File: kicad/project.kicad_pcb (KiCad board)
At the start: 2 copper layers, 58 x 58 mm, 40 parts, among them J1 Conn_01x05, J2 Conn_01x01, Q1 SI2323CDS, SW1 SW_SPDT, SW2 SW_SPDT, SW3 SW_Push, U1 STM32L031F4Px

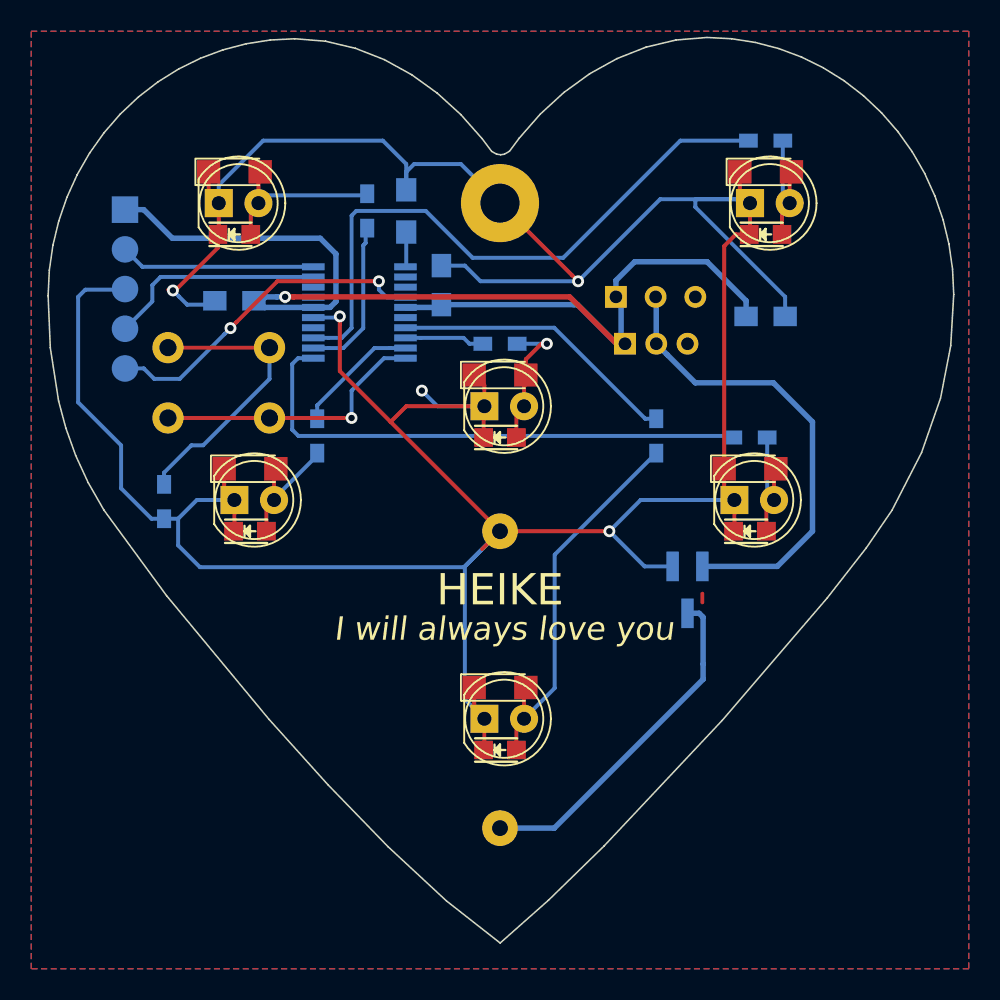
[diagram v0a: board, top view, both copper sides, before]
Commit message: Also fit the premade mould from China
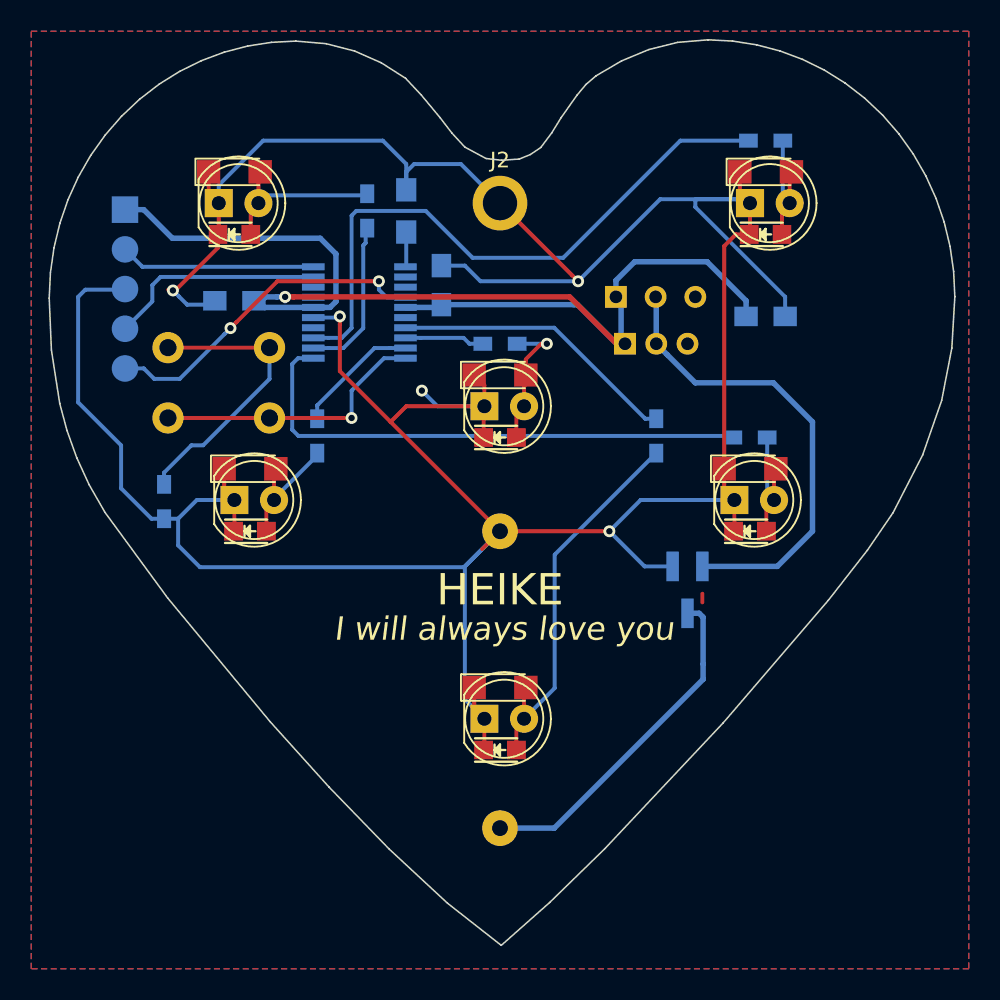
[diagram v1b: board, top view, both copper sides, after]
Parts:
- J1: footprint SWD_Header -> theapi:SWD_Header
- J2: footprint Mounting_Holes:MountingHole_2.5mm_Pad -> Mounting_Holes:MountingHole_2.2mm_M2_ISO7380_Pad
- moved REF** 15.9 mm to (140.5, 88.2)
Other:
- outline, holes or cut-outs redrawn

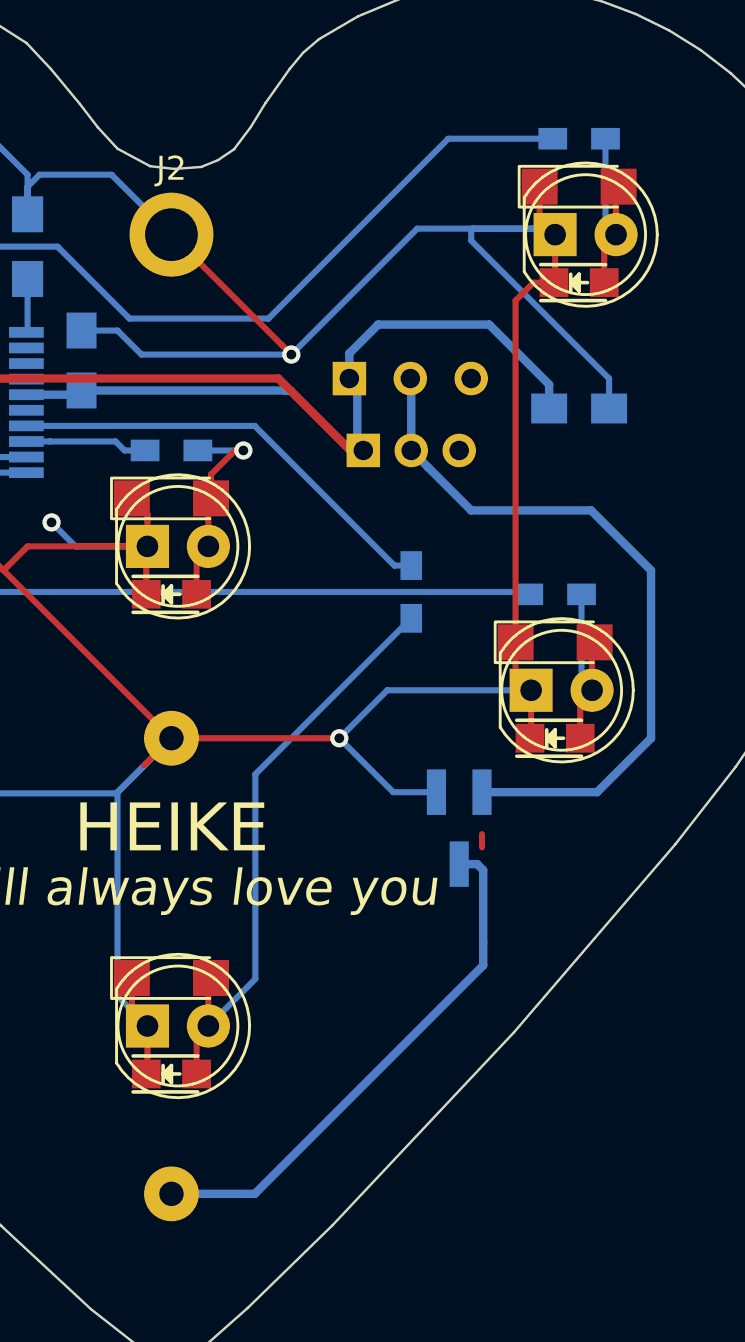
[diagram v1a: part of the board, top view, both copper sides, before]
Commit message: Moved the mosfet away from the battery
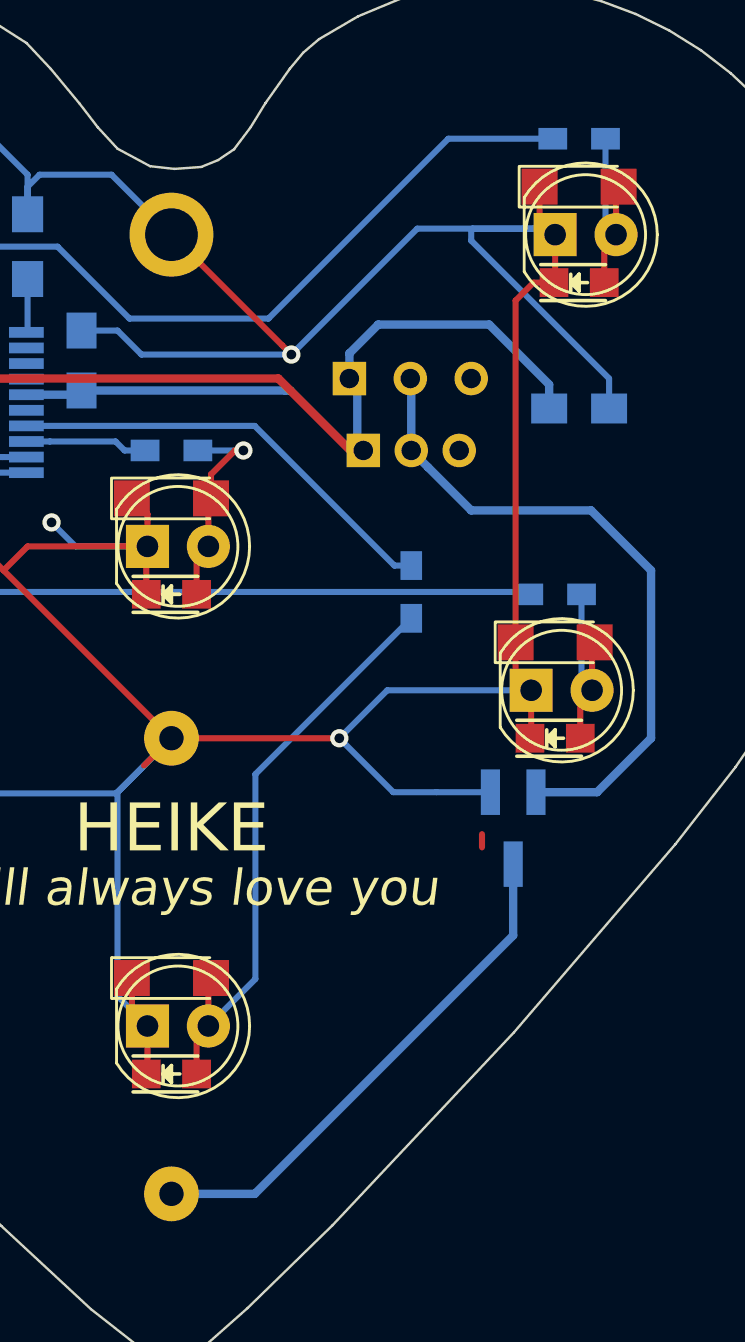
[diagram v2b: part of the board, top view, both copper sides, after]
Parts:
- moved Q1 2.25 mm to (144.2, 120.8)
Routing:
- net GND: track 233.2 -> 235.5 mm
- net /BATT_PROTECTED: track 30.1 -> 27.9 mm
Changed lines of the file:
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@@
     (links 69)
     (no_connects 0)
-    (area 101.09984 85.498481 159.15956 143.553153)
+    (area 97.899999 79.3 161.100001 148.700001)
     (thickness 1.6)
     (drawings 95)
-    (tracks 258)
+    (tracks 256)
     (zones 0)
     (modules 40)
@@
   )
   (module TO_SOT_Packages_SMD:SOT-23_Handsoldering (layer B.Cu)
-    (at 142 120.75 270)
+    (at 144.25 120.75 270)
     (descr "SOT-23, Handsoldering")
     (tags SOT-23)
@@
     (descr "Mounting Hole 2.2mm, M2, ISO7380")
     (tags "mounting hole 2.2mm m2 iso7380")
-    (fp_text reference J2 (at 0 -2.75) (layer F.SilkS)
+    (fp_text reference J2 (at 0 -2.75) (layer F.Fab)
       (effects (font (size 1 1) (thickness 0.15)))
     )
@@
   (gr_line (start 130 147) (end 130 82) (angle 90) (layer Cmts.User) (width 0.2))
   (segment (start 142.95 121) (end 142.95 121.55) (width 0.254) (layer F.Cu) (net 0))
+  (segment (start 141.05 119.25) (end 143.3 119.25) (width 0.254) (layer B.Cu) (net 1))
   (segment (start 145.096 95.75) (end 142.55 95.75) (width 0.254) (layer B.Cu) (net 1))
   (segment (start 142.55 95.75) (end 142.5 95.8) (width 0.254) (layer B.Cu) (net 1))
@@
   (segment (start 148.04902 98) (end 148.04902 96.49098) (width 0.254) (layer F.Cu) (net 22))
   (segment (start 148.04902 96.49098) (end 148.54 96) (width 0.254) (layer F.Cu) (net 22))
-  (segment (start 142.75 122.25) (end 142 122.25) (width 0.35) (layer B.Cu) (net 24))
   (segment (start 130 136) (end 133.475 136) (width 0.35) (layer B.Cu) (net 24))
-  (segment (start 133.475 136) (end 143 126.475) (width 0.35) (layer B.Cu) (net 24))
-  (segment (start 143 125.5) (end 143 122.5) (width 0.35) (layer B.Cu) (net 24))
-  (segment (start 143 122.5) (end 142.75 122.25) (width 0.35) (layer B.Cu) (net 24))
-  (segment (start 143 126.475) (end 143 125.5) (width 0.35) (layer B.Cu) (net 24))
+  (segment (start 133.475 136) (end 144.25 125.225) (width 0.35) (layer B.Cu) (net 24))
+  (segment (start 144.25 125.225) (end 144.25 122.25) (width 0.35) (layer B.Cu) (net 24))
   (segment (start 138 105) (end 137.75 104.75) (width 0.35) (layer B.Cu) (net 25))
   (segment (start 137.75 104.75) (end 137.75 102.33) (width 0.35) (layer B.Cu) (net 25))
@@
   (segment (start 120.5 109.75) (end 114.75 109.75) (width 0.254) (layer F.Cu) (net 28))
   (via (at 120.5 109.75) (size 0.762) (drill 0.4064) (layers F.Cu B.Cu) (net 28))
+  (segment (start 145.2 119.25) (end 147.75 119.25) (width 0.35) (layer B.Cu) (net 30))
   (segment (start 140 105) (end 140 102.04) (width 0.35) (layer B.Cu) (net 30))
   (segment (start 140 102.04) (end 139.96 102) (width 0.35) (layer B.Cu) (net 30))
-  (segment (start 142.95 119.25) (end 147.75 119.25) (width 0.35) (layer B.Cu) (net 30))
   (segment (start 150 110) (end 147.5 107.5) (width 0.35) (layer B.Cu) (net 30))
   (segment (start 147.75 119.25) (end 150 117) (width 0.35) (layer B.Cu) (net 30))

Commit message: Tidy up
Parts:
- R1: footprint Resistors_SMD:R_0805_HandSoldering -> Resistors_SMD:R_0603_HandSoldering
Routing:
- net (no net): track 0.55 -> 0.00 mm
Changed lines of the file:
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@@
     (thickness 1.6)
     (drawings 95)
-    (tracks 256)
+    (tracks 255)
     (zones 0)
     (modules 40)
@@
       (net 1 GND))
     (model LEDs.3dshapes/LED_0805.wrl
-      (at (xyz 0 0 0))
-      (scale (xyz 1 1 1))
-      (rotate (xyz 0 0 0))
-    )
-  )
-  (module Resistors_SMD:R_0805_HandSoldering (layer B.Cu)
-    (at 124 96.5 90)
-    (descr "Resistor SMD 0805, hand soldering")
-    (tags "resistor 0805")
-    (attr smd)
-    (fp_text reference R1 (at 0 2.1 90) (layer B.SilkS)
-      (effects (font (size 1 1) (thickness 0.15)) (justify mirror))
-    )
-    (fp_text value 10K (at 0 -2.1 90) (layer B.Fab)
-      (effects (font (size 1 1) (thickness 0.15)) (justify mirror))
-    )
-    (fp_line (start -1 -0.625) (end -1 0.625) (layer B.Fab) (width 0.1))
-    (fp_line (start 1 -0.625) (end -1 -0.625) (layer B.Fab) (width 0.1))
-    (fp_line (start 1 0.625) (end 1 -0.625) (layer B.Fab) (width 0.1))
-    (fp_line (start -1 0.625) (end 1 0.625) (layer B.Fab) (width 0.1))
-    (fp_line (start -2.4 1) (end 2.4 1) (layer B.CrtYd) (width 0.05))
-    (fp_line (start -2.4 -1) (end 2.4 -1) (layer B.CrtYd) (width 0.05))
-    (fp_line (start -2.4 1) (end -2.4 -1) (layer B.CrtYd) (width 0.05))
-    (fp_line (start 2.4 1) (end 2.4 -1) (layer B.CrtYd) (width 0.05))
-    (fp_line (start 0.6 -0.875) (end -0.6 -0.875) (layer B.SilkS) (width 0.15))
-    (fp_line (start -0.6 0.875) (end 0.6 0.875) (layer B.SilkS) (width 0.15))
-    (pad 1 smd rect (at -1.35 0 90) (size 1.5 1.3) (layers B.Cu B.Paste B.Mask)
-      (net 6 "Net-(R1-Pad1)"))
-    (pad 2 smd rect (at 1.35 0 90) (size 1.5 1.3) (layers B.Cu B.Paste B.Mask)
-      (net 1 GND))
-    (model Resistors_SMD.3dshapes/R_0805_HandSoldering.wrl
       (at (xyz 0 0 0))
       (scale (xyz 1 1 1))
@@
       (net 1 GND))
   )
+  (module Resistors_SMD:R_0603_HandSoldering (layer B.Cu)
+    (at 124 96.5 90)
+    (descr "Resistor SMD 0603, hand soldering")
+    (tags "resistor 0603")
+    (attr smd)
+    (fp_text reference R1 (at 0 1.45 90) (layer B.SilkS)
+      (effects (font (size 1 1) (thickness 0.15)) (justify mirror))
+    )
+    (fp_text value 10K (at 0 -1.55 90) (layer B.Fab)
+      (effects (font (size 1 1) (thickness 0.15)) (justify mirror))
+    )
+    (fp_text user %R (at 0 0 90) (layer B.Fab)
+      (effects (font (size 0.4 0.4) (thickness 0.075)) (justify mirror))
+    )
+    (fp_line (start -0.8 -0.4) (end -0.8 0.4) (layer B.Fab) (width 0.1))
+    (fp_line (start 0.8 -0.4) (end -0.8 -0.4) (layer B.Fab) (width 0.1))
+    (fp_line (start 0.8 0.4) (end 0.8 -0.4) (layer B.Fab) (width 0.1))
+    (fp_line (start -0.8 0.4) (end 0.8 0.4) (layer B.Fab) (width 0.1))
+    (fp_line (start 0.5 -0.68) (end -0.5 -0.68) (layer B.SilkS) (width 0.12))
+    (fp_line (start -0.5 0.68) (end 0.5 0.68) (layer B.SilkS) (width 0.12))
+    (fp_line (start -1.96 0.7) (end 1.95 0.7) (layer B.CrtYd) (width 0.05))
+    (fp_line (start -1.96 0.7) (end -1.96 -0.7) (layer B.CrtYd) (width 0.05))
+    (fp_line (start 1.95 -0.7) (end 1.95 0.7) (layer B.CrtYd) (width 0.05))
+    (fp_line (start 1.95 -0.7) (end -1.96 -0.7) (layer B.CrtYd) (width 0.05))
+    (pad 1 smd rect (at -1.1 0 90) (size 1.2 0.9) (layers B.Cu B.Paste B.Mask)
+      (net 6 "Net-(R1-Pad1)"))
+    (pad 2 smd rect (at 1.1 0 90) (size 1.2 0.9) (layers B.Cu B.Paste B.Mask)
+      (net 1 GND))
+    (model ${KISYS3DMOD}/Resistors_SMD.3dshapes/R_0603.wrl
+      (at (xyz 0 0 0))
+      (scale (xyz 1 1 1))
+      (rotate (xyz 0 0 0))
+    )
+  )
   (gr_line (start 143.324659 85.548502) (end 141.371726 85.711999) (layer Edge.Cuts) (width 0.1))
   (gr_line (start 129.109149 93.145392) (end 127.751555 92.416432) (layer Edge.Cuts) (width 0.1))
@@
   (gr_line (start 99 115) (end 161 115) (angle 90) (layer Cmts.User) (width 0.2))
   (gr_line (start 130 147) (end 130 82) (angle 90) (layer Cmts.User) (width 0.2))
-  (segment (start 142.95 121) (end 142.95 121.55) (width 0.254) (layer F.Cu) (net 0))
   (segment (start 141.05 119.25) (end 143.3 119.25) (width 0.254) (layer B.Cu) (net 1))
   (segment (start 145.096 95.75) (end 142.55 95.75) (width 0.254) (layer B.Cu) (net 1))

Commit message: Solder mask between pins of the stm32
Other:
- board text added: "+"
- board text added: "-"
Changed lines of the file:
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@@
-(kicad_pcb (version 4) (host pcbnew 4.0.7-e2-6376~58~ubuntu16.04.1)
+(kicad_pcb (version 4) (host pcbnew 4.0.6)
   (general
     (links 69)
     (no_connects 0)
-    (area 97.899999 79.3 161.100001 148.700001)
+    (area 101.09984 85.498481 159.15956 143.553153)
     (thickness 1.6)
-    (drawings 95)
+    (drawings 101)
     (tracks 255)
     (zones 0)
@@
     )
   )
+  (gr_text - (at 143.1 95.9) (layer F.SilkS)
+    (effects (font (size 1 1) (thickness 0.15)) (justify left))
+  )
+  (gr_text - (at 110.3 114.9) (layer F.SilkS)
+    (effects (font (size 1 1) (thickness 0.15)) (justify left))
+  )
+  (gr_text - (at 142.3 114.9) (layer F.SilkS)
+    (effects (font (size 1 1) (thickness 0.15)) (justify left))
+  )
+  (gr_text - (at 126.3 108.9) (layer F.SilkS)
+    (effects (font (size 1 1) (thickness 0.15)) (justify left))
+  )
+  (gr_text - (at 109.4 96.1) (layer F.SilkS)
+    (effects (font (size 1 1) (thickness 0.15)) (justify left))
+  )
+  (gr_text + (at 116.5 96) (layer F.SilkS)
+    (effects (font (size 1 1) (thickness 0.15)) (justify left))
+  )
   (gr_line (start 143.324659 85.548502) (end 141.371726 85.711999) (layer Edge.Cuts) (width 0.1))
